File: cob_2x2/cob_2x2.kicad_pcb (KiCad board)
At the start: 2 copper layers, 158 x 158 mm, 114 parts, among them J1 Conn_01x02, J3 Anderson_two_redblack, J4 Conn_01x06_Female, J5 Conn_01x06_Male, U1 5V_REG, U10 AL8860, U11 3_Inverter, U2 AL8860, U22 AL8860, U23 AL8860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

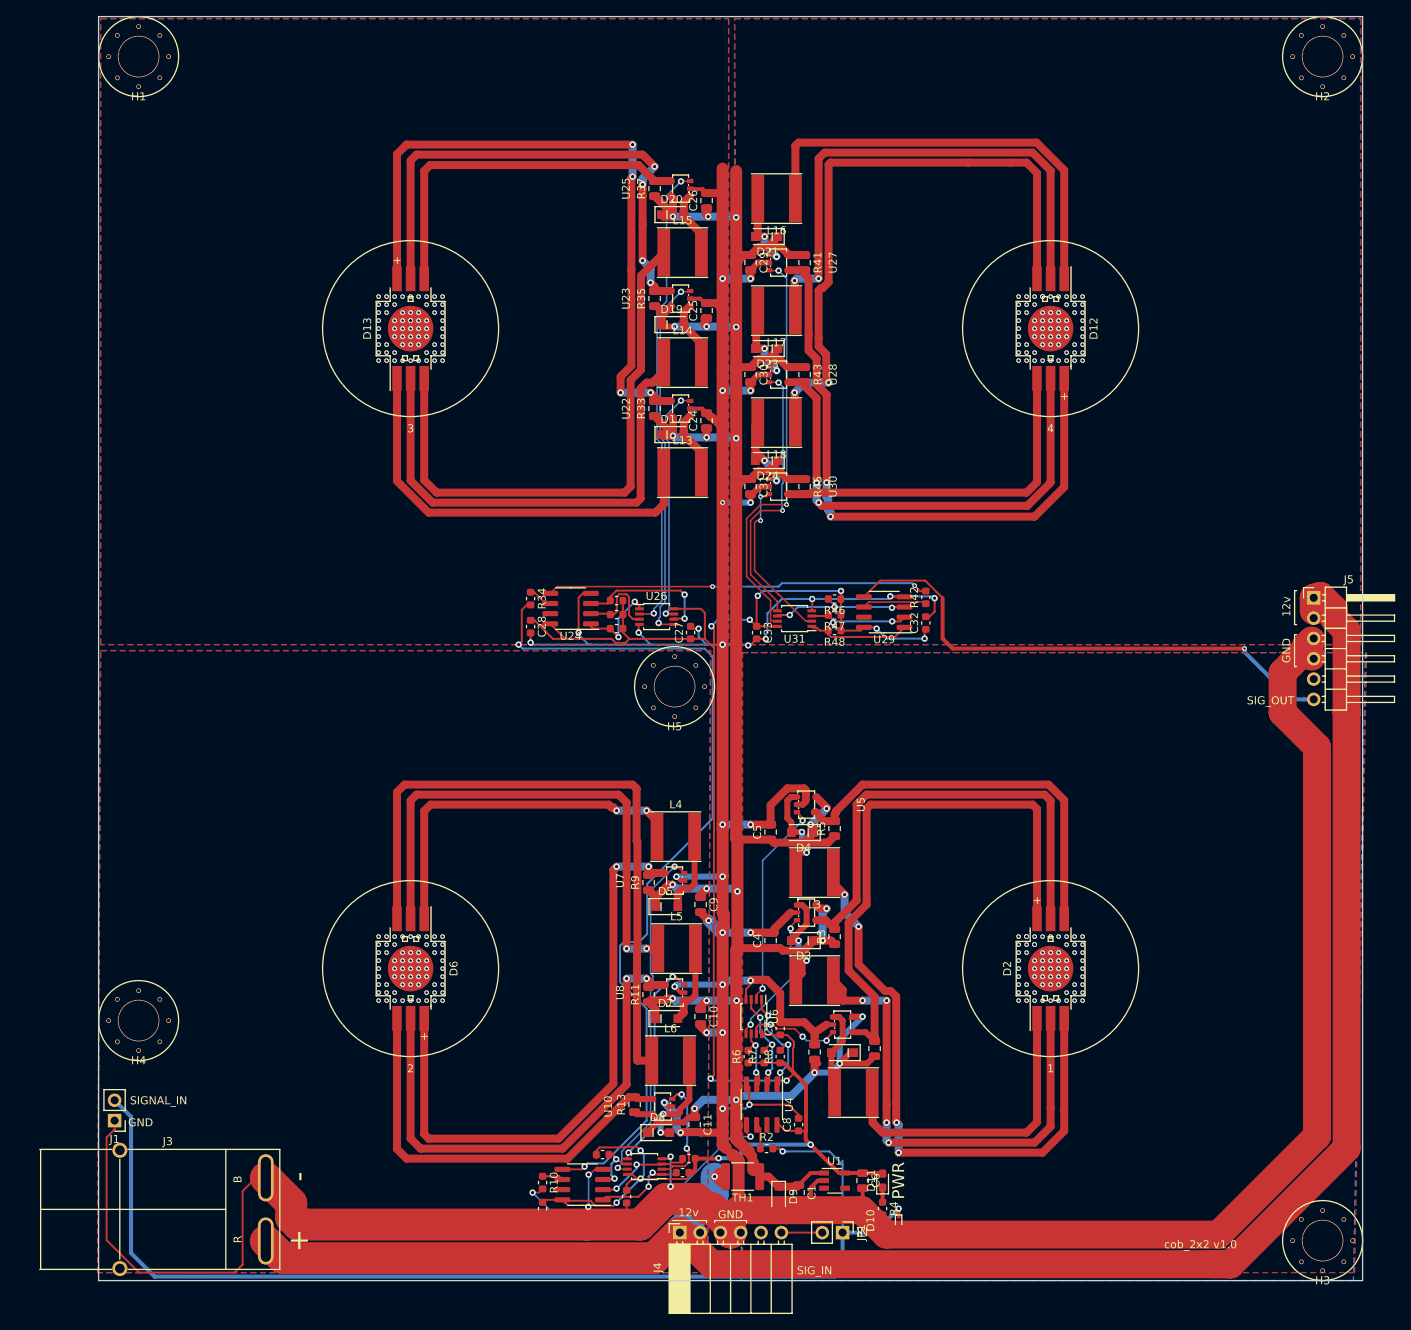
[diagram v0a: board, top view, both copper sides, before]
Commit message: cob_2x2 v1.1:
- Fix inverter footprint
- Increase size of 5V TVS diode to SOD-523
- Increase clearance for mounting holes by 1mm
- Make mounting holes evenly spaced
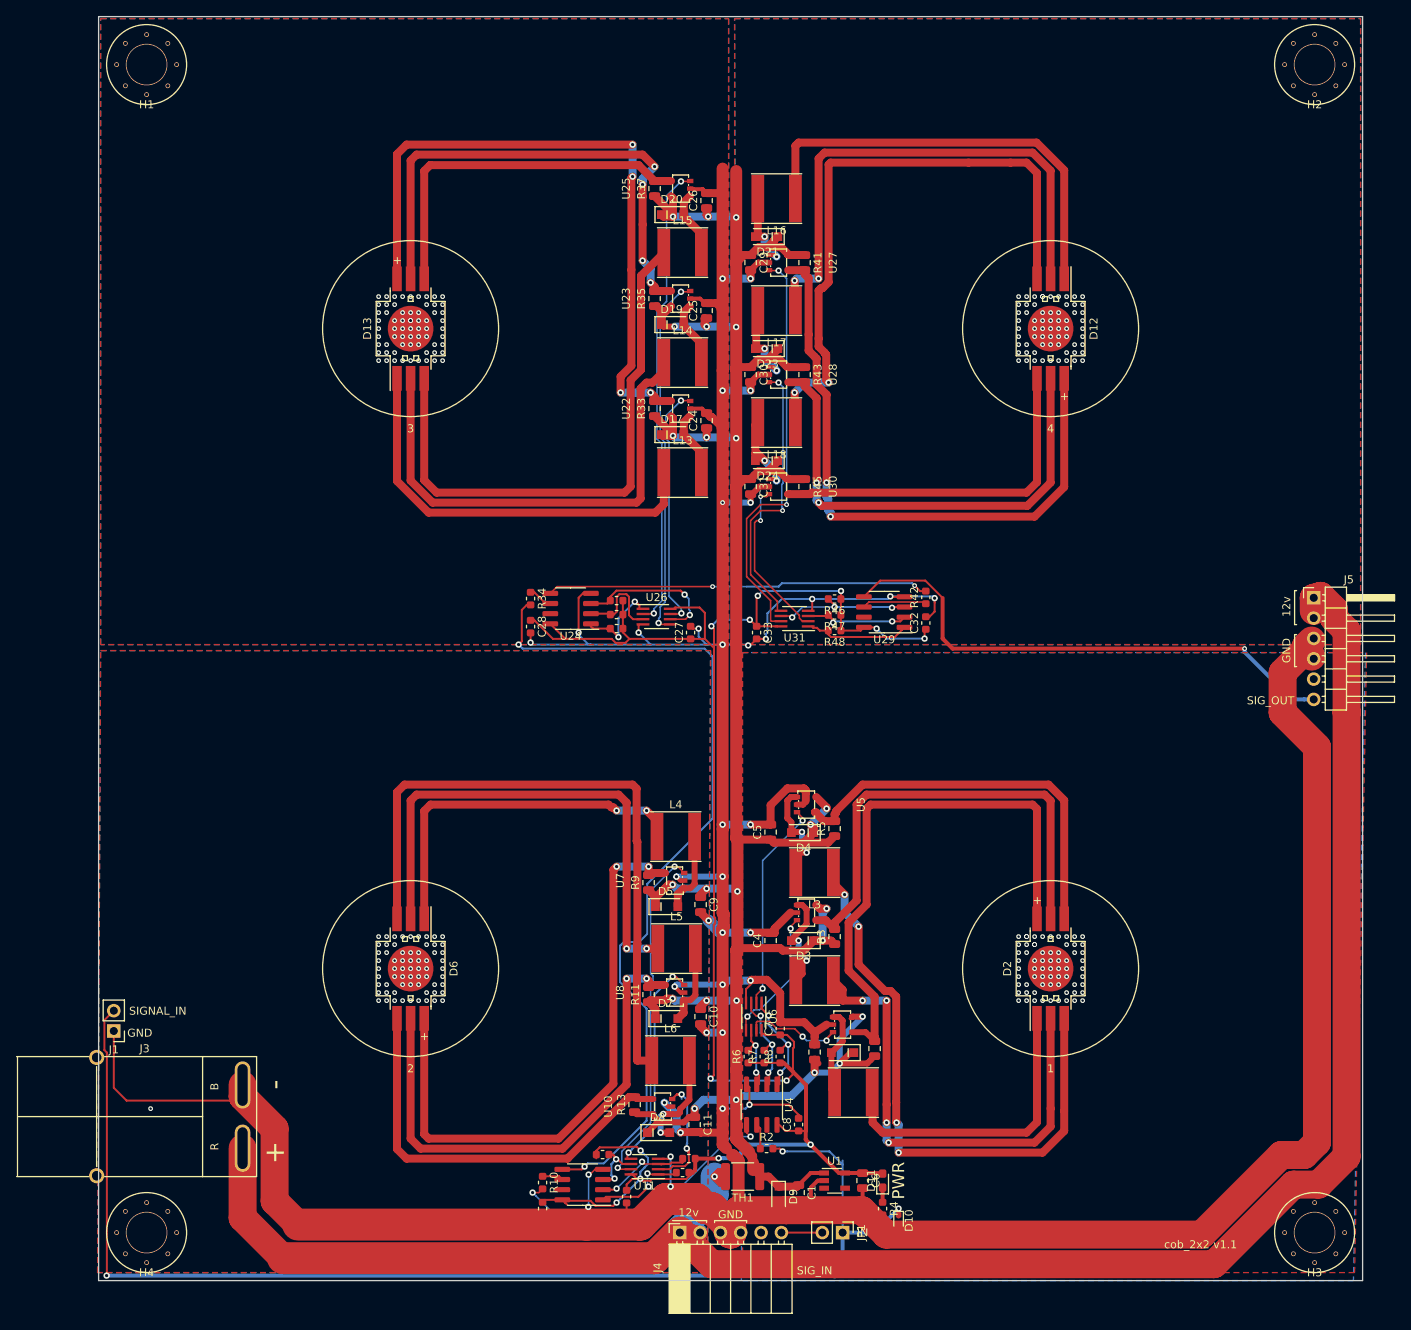
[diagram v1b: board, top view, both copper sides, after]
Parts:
- removed H5: MountingHole, homebrew:HOLE_5MM_#8
- D10: footprint homebrew:SOD-923 -> Diode_SMD:D_SOD-523
- U1: value 5V_REG -> 5V_REG_AP7370-50W5-7
- U10, U2, U22, U23, U27, U28, U3, U30, U5, U7, U8: value AL8860 -> AL8860_LED_DRIVER
- U11, U26, U31, U6: value 3_Inverter -> 3_Inverter_TC7WH14FU,LJ(CT; footprint Package_SO:TSSOP-8_3x3mm_P0.65mm -> Package_SO:SSOP-8_2.95x2.8mm_P0.65mm
- moved H4 26.5 mm to (107.0, 253.0)
- moved J3 12.0 mm to (119.0, 238.5)
- moved J1 11.2 mm to (102.9, 227.8)
- moved H1 1.41 mm to (107.0, 107.0)
- moved H2 1.41 mm to (253.0, 107.0)
- moved H3 1.41 mm to (253.0, 253.0)
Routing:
- net SIGNAL_IN: track 142.8 -> 158.5 mm, vias 2 -> 3
- net 12V_RAW: track 239.5 -> 250.5 mm
- net GND: track 628.3 -> 618.4 mm
- net /sheet5DF1A510/R_SIGNAL: track 29.9 -> 31.7 mm
- net /sheet5DF1A510/B_INVERTED: track 17.2 -> 18.4 mm
- net /single_led/G_INVERTED: track 13.3 -> 14.3 mm
- net /single_led/R_SIGNAL: track 12.0 -> 13.0 mm, vias 3 -> 2
- net /sheet5DF187B4/R_INVERTED: track 11.5 -> 12.3 mm
- net /single_led/R_INVERTED: track 14.5 -> 13.7 mm
- net +5V: track 241.4 -> 242.2 mm
- net /single_led/G_SIGNAL: track 16.8 -> 17.4 mm
- net /sheet5DF1FB98/B_SIGNAL: track 20.8 -> 21.3 mm
- net /sheet5DF187B4/B_LED_A: vias 65 -> 66
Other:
- board text added: "cob_2x2 v1.1"
- board text removed: "cob_2x2 v1.0"
